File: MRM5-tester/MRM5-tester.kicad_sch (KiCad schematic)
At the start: 1 part, among them Q1 IRFB7545

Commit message: tester updated
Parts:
- removed Q1: IRFB7545, PCM_Package_TO_SOT_THT_AKL:TO-220-3_Vertical_GDS, symbol PCM_Transistor_MOSFET_AKL:IRFB7545
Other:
- added sheet analog (analog.kicad_sch)
- added sheet interface (interface.kicad_sch)
- added sheet mcu (mcu.kicad_sch)
- added sheet power (power.kicad_sch)
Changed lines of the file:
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@@
 	(generator_version "8.0")
 	(paper "A4")
-	(symbol
-		(lib_id "PCM_Transistor_MOSFET_AKL:IRFB7545")
-		(at 69.85 68.58 0)
-		(unit 1)
-		(exclude_from_sim no)
-		(in_bom yes)
-		(on_board yes)
-		(dnp no)
+	(sheet
+		(at 78.74 53.34)
+		(size 38.1 41.91)
 		(fields_autoplaced yes)
-		(property "Reference" "Q1"
-			(at 76.2 67.3099 0)
+		(stroke
+			(width 0.1524)
+			(type solid)
+		)
+		(fill
+			(color 0 0 0 0.0000)
+		)
+		(property "Sheetname" "mcu"
+			(at 78.74 52.6284 0)
 			(effects
 				(font
 					(size 1.27 1.27)
 				)
-				(justify left)
+				(justify left bottom)
 			)
 		)
-		(property "Value" "IRFB7545"
-			(at 76.2 69.8499 0)
+		(property "Sheetfile" "mcu.kicad_sch"
+			(at 78.74 95.8346 0)
 			(effects
 				(font
 					(size 1.27 1.27)
 				)
-				(justify left)
+				(justify left top)
 			)
 		)
-		(property "Footprint" "PCM_Package_TO_SOT_THT_AKL:TO-220-3_Vertical_GDS"
-			(at 74.93 66.04 0)
+		(instances
+			(project "MRM5-tester"
+				(path "/6e775c75-0b09-4e5f-9bff-c5585ac94ad7"
+					(page "2")
+				)
+			)
+		)
+	)
+	(sheet
+		(at 199.39 55.88)
+		(size 44.45 46.99)
+		(fields_autoplaced yes)
+		(stroke
+			(width 0.1524)
+			(type solid)
+		)
+		(fill
+			(color 0 0 0 0.0000)
+		)
+		(property "Sheetname" "interface"
+			(at 199.39 55.1684 0)
 			(effects
 				(font
 					(size 1.27 1.27)
 				)
-				(hide yes)
+				(justify left bottom)
 			)
 		)
-		(property "Datasheet" "https://www.tme.eu/Document/640fad67548da8e6315008b5d56757f2/irfb7545pbf.pdf"
-			(at 69.85 68.58 0)
+		(property "Sheetfile" "interface.kicad_sch"
+			(at 199.39 103.4546 0)
 			(effects
 				(font
 					(size 1.27 1.27)
 				)
-				(hide yes)
+				(justify left top)
 			)
 		)
-		(property "Description" "TO-220 N-MOSFET enchancement mode transistor, 60V, 95A, 125W, Alternate KiCAD Library"
-			(at 69.85 68.58 0)
+		(instances
+			(project "MRM5-tester"
+				(path "/6e775c75-0b09-4e5f-9bff-c5585ac94ad7"
+					(page "3")
+				)
+			)
+		)
+	)
+	(sheet
+		(at 176.53 123.19)
+		(size 59.69 25.4)
+		(fields_autoplaced yes)
+		(stroke
+			(width 0.1524)
+			(type solid)
+		)
+		(fill
+			(color 0 0 0 0.0000)
+		)
+		(property "Sheetname" "power"
+			(at 176.53 122.4784 0)
 			(effects
 				(font
 					(size 1.27 1.27)
 				)
-				(hide yes)
+				(justify left bottom)
 			)
 		)
-		(pin "2"
-		)
-		(pin "1"
-		)
-		(pin "3"
+		(property "Sheetfile" "power.kicad_sch"
+			(at 176.53 149.1746 0)
+			(effects
+				(font
+					(size 1.27 1.27)
+				)
+				(justify left top)
+			)
 		)
 		(instances
-			(project ""
+			(project "MRM5-tester"
 				(path "/6e775c75-0b09-4e5f-9bff-c5585ac94ad7"
-					(reference "Q1")
-					(unit 1)
+					(page "5")
 				)
 			)
+		)
+	)
+	(sheet
+		(at 59.69 127)
+		(size 39.37 45.72)
+		(fields_autoplaced yes)
+		(stroke
+			(width 0.1524)
+			(type solid)
+		)
+		(fill
+			(color 0 0 0 0.0000)
+		)
+		(property "Sheetname" "analog"
+			(at 59.69 126.2884 0)
+			(effects
+				(font
+					(size 1.27 1.27)
+				)
+				(justify left bottom)
+			)
+		)
+		(property "Sheetfile" "analog.kicad_sch"
+			(at 59.69 173.3046 0)
+			(effects
+				(font
+					(size 1.27 1.27)
+				)
+				(justify left top)
+			)
+		)
+		(instances
+			(project "MRM5-tester"
+				(path "/6e775c75-0b09-4e5f-9bff-c5585ac94ad7"
+					(page "4")
+				)
+			)

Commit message: tester PCB 작성중
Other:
- sheet analog ports: added 1V6, 3V3, GND, Vn_h, Vp_sh, Z_IFlag, Z_TFlag, sigV, sigZ; removed none
- sheet interface ports: added 3V3, 5V, GND, STLINK_CLK, STLINK_DIO, STLINK_RST, SUSPEND, SYNC, UART_CTS, UART_RTS, UART_RXD, UART_TXD, Vn_h, Vp_h, WAKEUP; removed none
- sheet mcu ports: added 1V6, 1V6_IFlag, 1V6_TFlag, ADC_V, DAC_Z, GND, MCU_NRST, MCU_SW_CLK, MCU_SW_DIO, MCU_UART_CTS, MCU_UART_RTS, MCU_UART_RX, MCU_UART_TX, SUSPEND, SYNC_INT, VDD, WAKEUP, Z_IFlag, Z_TFlag; removed none
- sheet power ports: added 1V6, 1V6_IFlag, 1V6_TFlag, 3V3, 5V, GND, Vn_h, Vp_h, Vp_sh; removed none

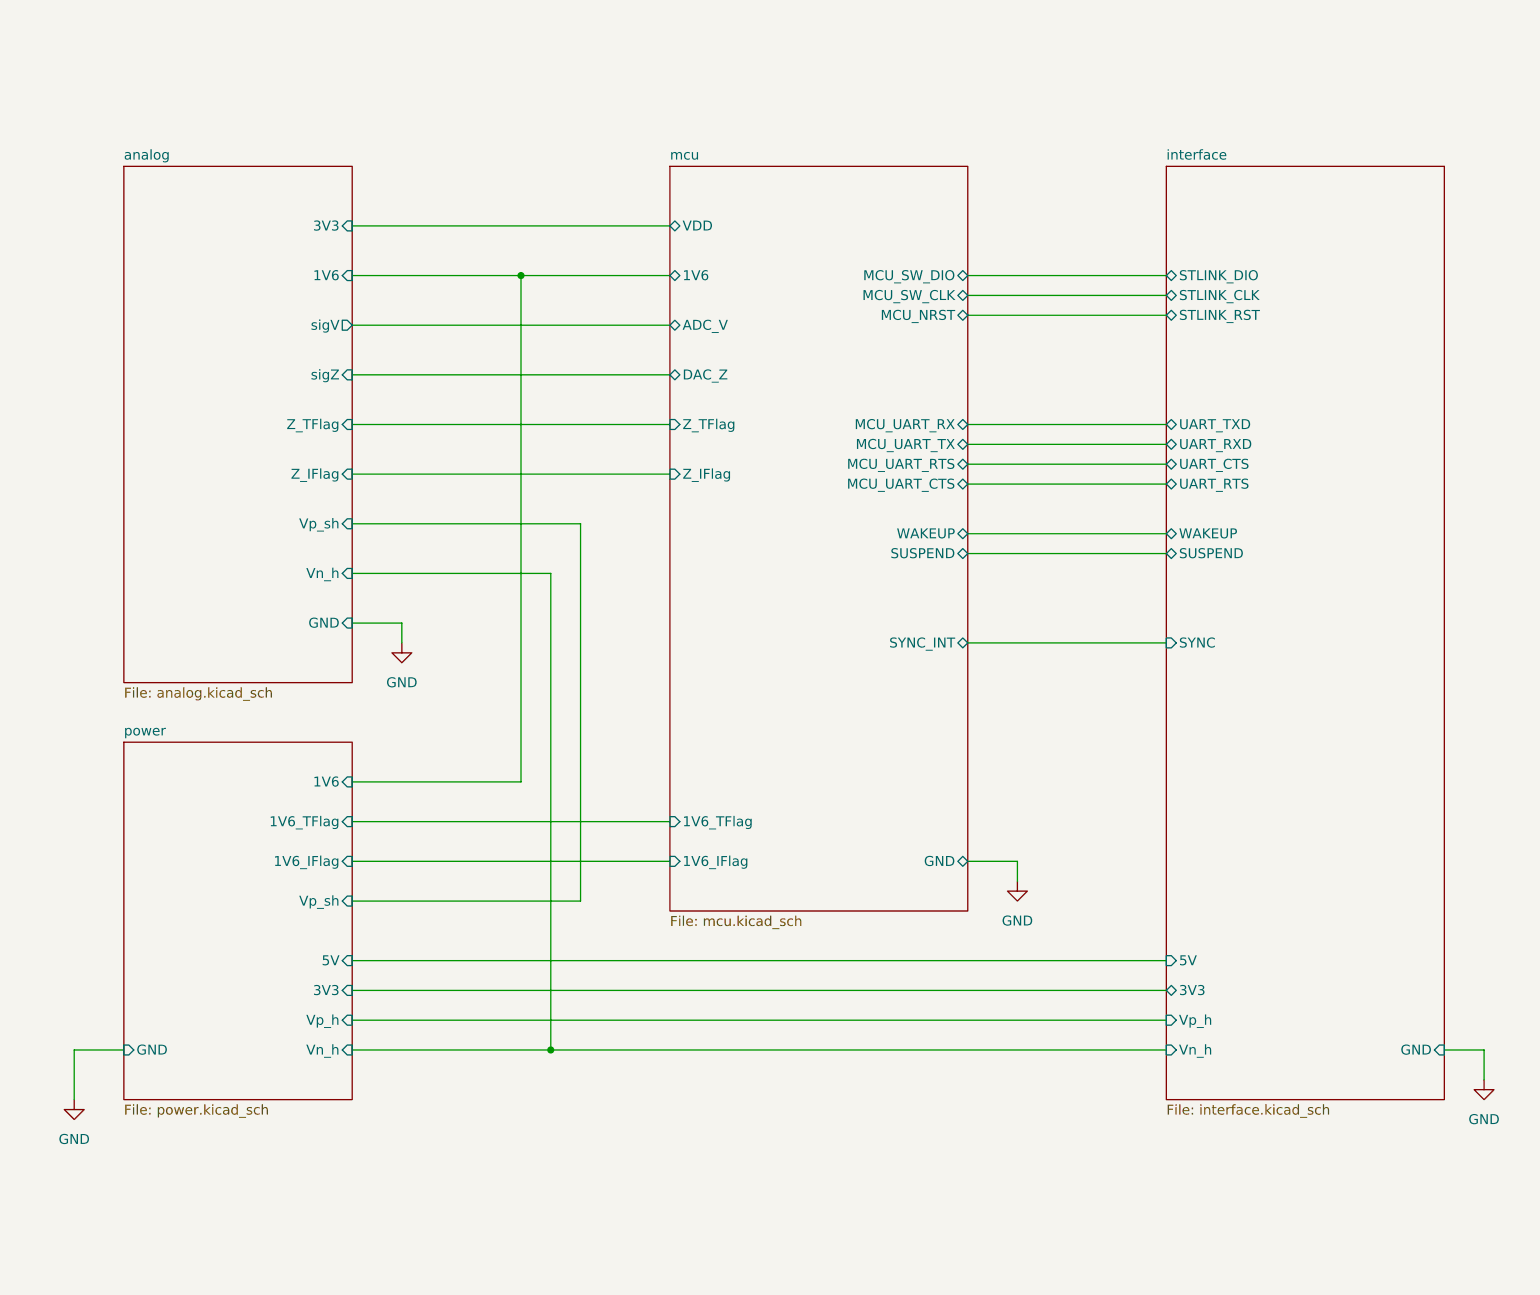
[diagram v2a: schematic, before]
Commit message: tester pcb 디자인 완료
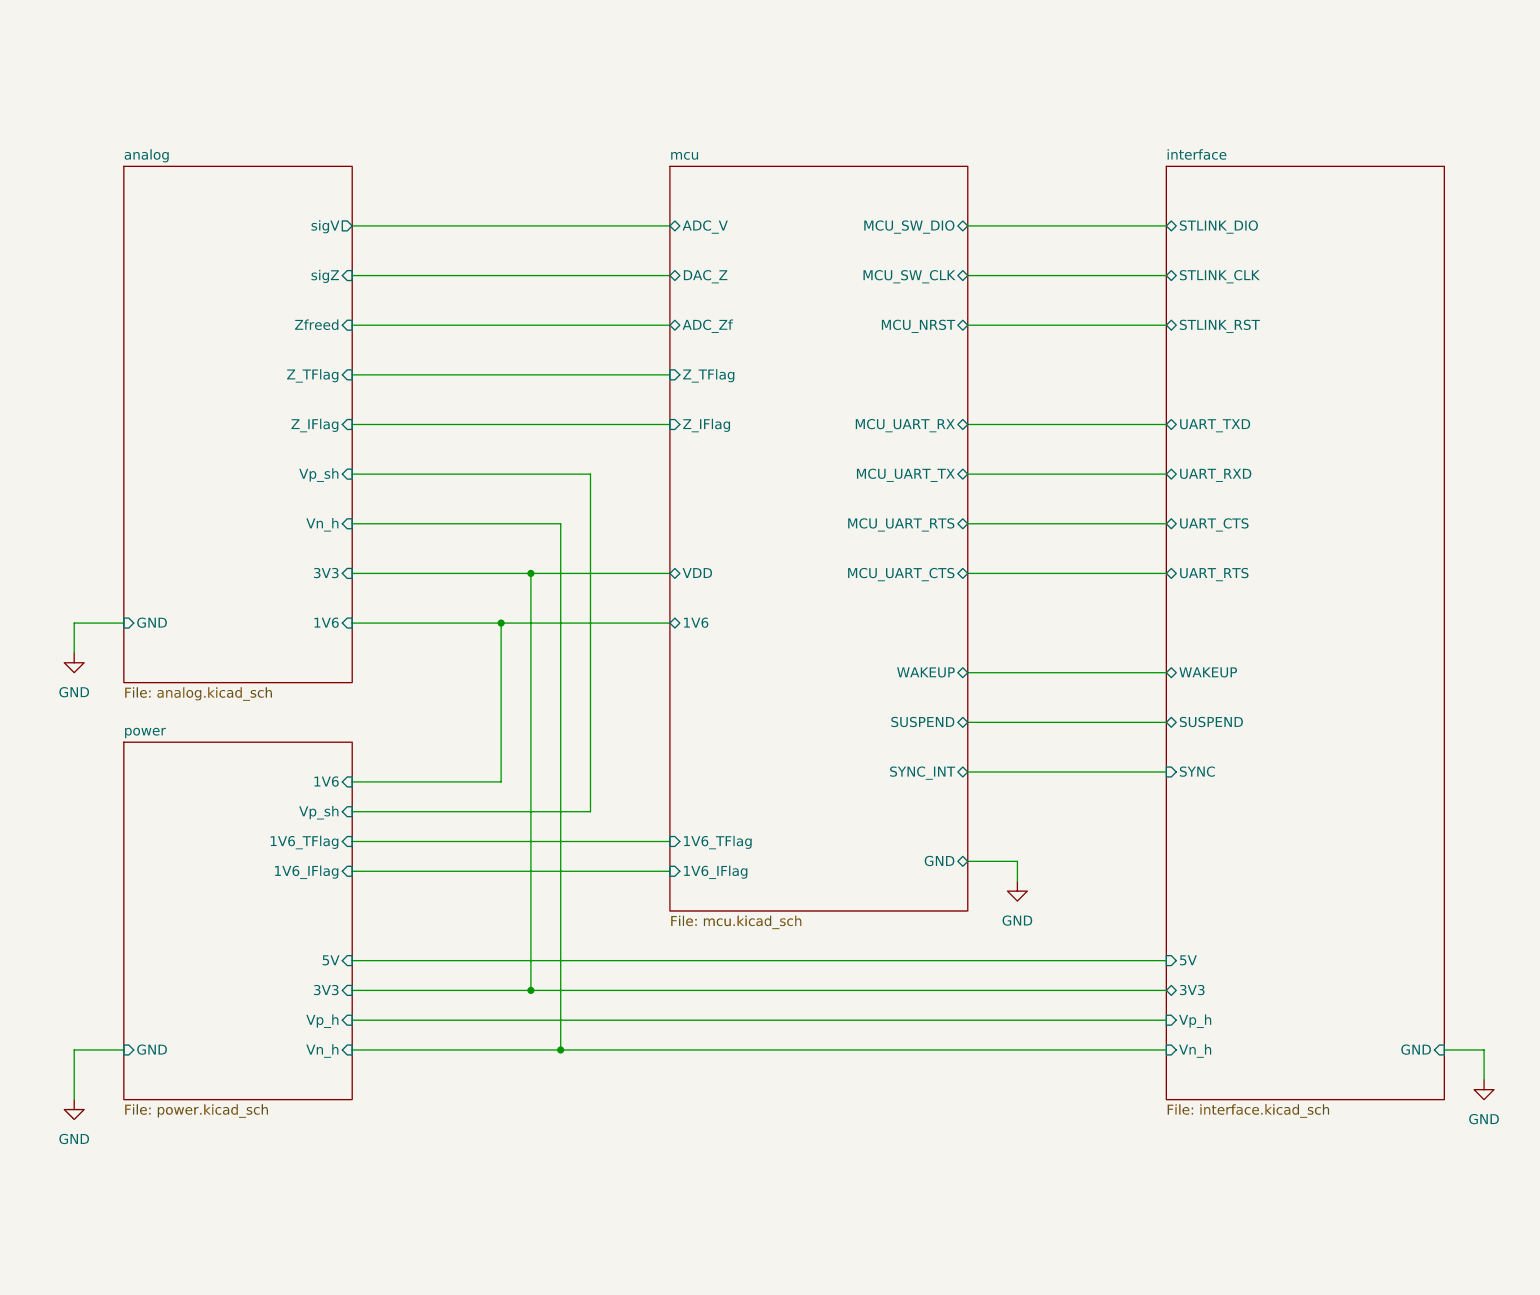
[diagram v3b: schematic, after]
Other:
- sheet analog ports: added Zfreed; removed none
- sheet mcu ports: added ADC_Zf; removed none

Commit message: tester PCB 검토
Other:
- sheet interface ports: added PUSH_BTN; removed WAKEUP
- sheet mcu ports: added PUSH_BTN; removed WAKEUP
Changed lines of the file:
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@@
-			)
-		)
-		(pin "WAKEUP" bidirectional
-			(at 172.72 97.79 0)
-			(effects
-				(font
-					(size 1.27 1.27)
-				)
-				(justify right)
 			)
 		)
@@
 				)
 				(justify left)
+			)
+		)
+		(pin "PUSH_BTN" bidirectional
+			(at 172.72 97.79 0)
+			(effects
+				(font
+					(size 1.27 1.27)
+				)
+				(justify right)
 			)
 		)
@@
 		(pin "UART_CTS" bidirectional
 			(at 198.12 78.74 180)
-			(effects
-				(font
-					(size 1.27 1.27)
-				)
-				(justify left)
-			)
-		)
-		(pin "WAKEUP" bidirectional
-			(at 198.12 97.79 180)
 			(effects
 				(font
@@
 			(effects
 				(font
+					(size 1.27 1.27)
+				)
+				(justify left)
+			)
+		)
+		(pin "PUSH_BTN" bidirectional
+			(at 198.12 97.79 180)
+			(effects
+				(font

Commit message: tester pcb updated
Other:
- sheet analog ports: added V2n, V2p; removed none
- sheet interface ports: added V2n, V2p; removed none

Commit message: 케이스에 마춰서 제작 중
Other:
- sheet analog ports: added PT1, PT2; removed none
- sheet interface ports: added PT1, PT2; removed none
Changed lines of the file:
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@@
+	(wire
+		(pts
+			(xy 90.17 31.75) (xy 194.31 31.75)
+		)
+		(stroke
+			(width 0)
+			(type default)
+		)
+	)
 	(wire
 		(pts
@@
 	(wire
 		(pts
-			(xy 90.17 29.21) (xy 194.31 29.21)
+			(xy 90.17 21.59) (xy 194.31 21.59)
 		)
 		(stroke
@@
 	(wire
 		(pts
-			(xy 90.17 33.02) (xy 194.31 33.02)
+			(xy 90.17 25.4) (xy 194.31 25.4)
 		)
 		(stroke
@@
 		(pts
 			(xy 90.17 73.66) (xy 130.81 73.66)
+		)
+		(stroke
+			(width 0)
+			(type default)
+		)
+	)
+	(wire
+		(pts
+			(xy 90.17 35.56) (xy 194.31 35.56)
 		)
 		(stroke
@@
 	)
 	(sheet
-		(at 194.31 22.86)
-		(size 35.56 137.16)
+		(at 194.31 16.51)
+		(size 35.56 143.51)
 		(fields_autoplaced yes)
 		(stroke
@@
 		)
 		(property "Sheetname" "interface"
-			(at 194.31 22.1484 0)
+			(at 194.31 15.7984 0)
 			(effects
 				(font
@@
 		)
 		(pin "V2n" input
-			(at 194.31 33.02 180)
+			(at 194.31 25.4 180)
 			(effects
 				(font
@@
 		)
 		(pin "V2p" input
-			(at 194.31 29.21 180)
+			(at 194.31 21.59 180)
+			(effects
+				(font
+					(size 1.27 1.27)
+				)
+				(justify left)
+			)
+		)
+		(pin "PT2" input
+			(at 194.31 35.56 180)
+			(effects
+				(font
+					(size 1.27 1.27)
+				)
+				(justify left)
+			)
+		)
+		(pin "PT1" input
+			(at 194.31 31.75 180)
 			(effects
 				(font
@@
 	)
 	(sheet
-		(at 60.96 22.86)
-		(size 29.21 83.82)
+		(at 60.96 16.51)
+		(size 29.21 90.17)
 		(fields_autoplaced yes)
 		(stroke
@@
 		)
 		(property "Sheetname" "analog"
-			(at 60.96 22.1484 0)
+			(at 60.96 15.7984 0)
 			(effects
 				(font
@@
 		)
 		(pin "V2p" input
-			(at 90.17 29.21 0)
+			(at 90.17 21.59 0)
 			(effects
 				(font
@@
 		)
 		(pin "V2n" input
-			(at 90.17 33.02 0)
-			(effects
-				(font
+			(at 90.17 25.4 0)
+			(effects
+				(font
+					(size 1.27 1.27)
+				)
+				(justify right)
+			)
+		)
+		(pin "PT1" input
+			(at 90.17 31.75 0)
+			(effects
+				(font
+					(size 1.27 1.27)
+				)
+				(justify right)
+			)
+		)
+		(pin "PT2" input
+			(at 90.17 35.56 0)
+			(effects
+				(font

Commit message: 1차 마감
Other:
- sheet analog ports: added PT1_bot, PT2_bot; removed none
- sheet interface ports: added 5V_bot, GND_bot, PT1_bot, PT2_bot; removed none
- sheet power ports: added 5V_bot, GND_bot; removed none
